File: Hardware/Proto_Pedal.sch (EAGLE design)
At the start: 124 parts, among them J1 POWER_JACKSMD_FIXED, Q1 2.5A/30V, SW1 SWITCH-3PDT

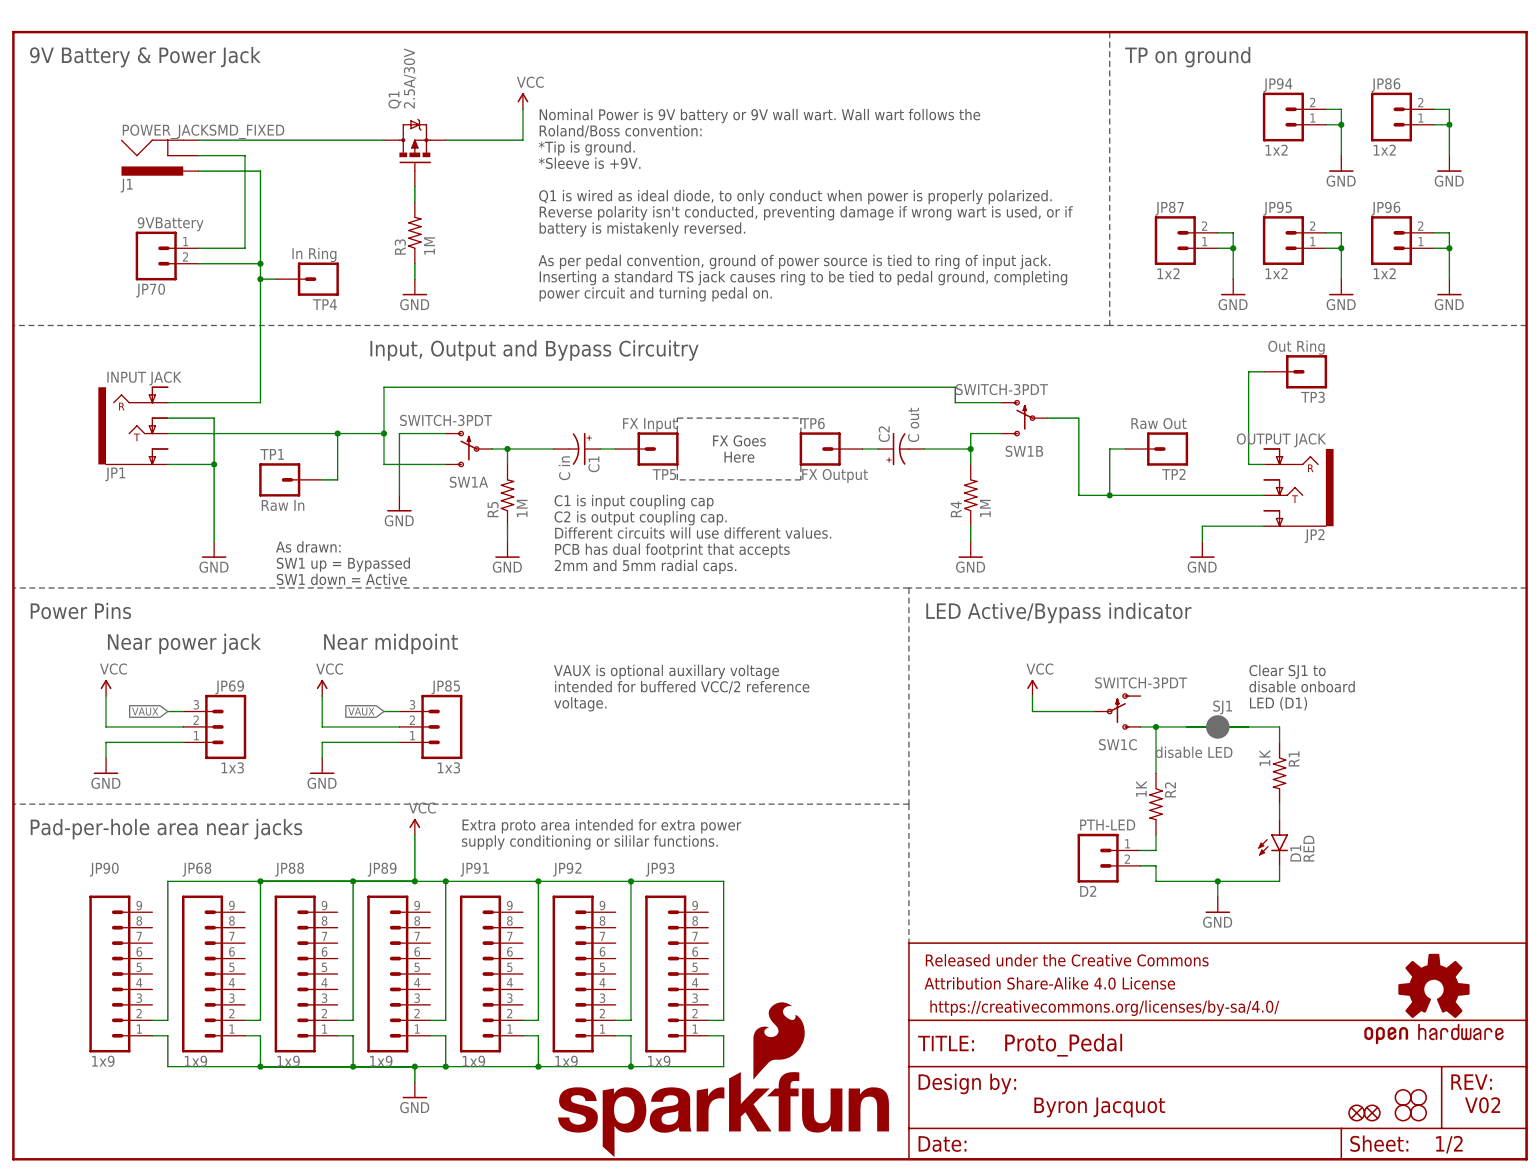
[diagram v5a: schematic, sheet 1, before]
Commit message: Updates after group review.
PTH power connector.
PTH LED bias resistor.
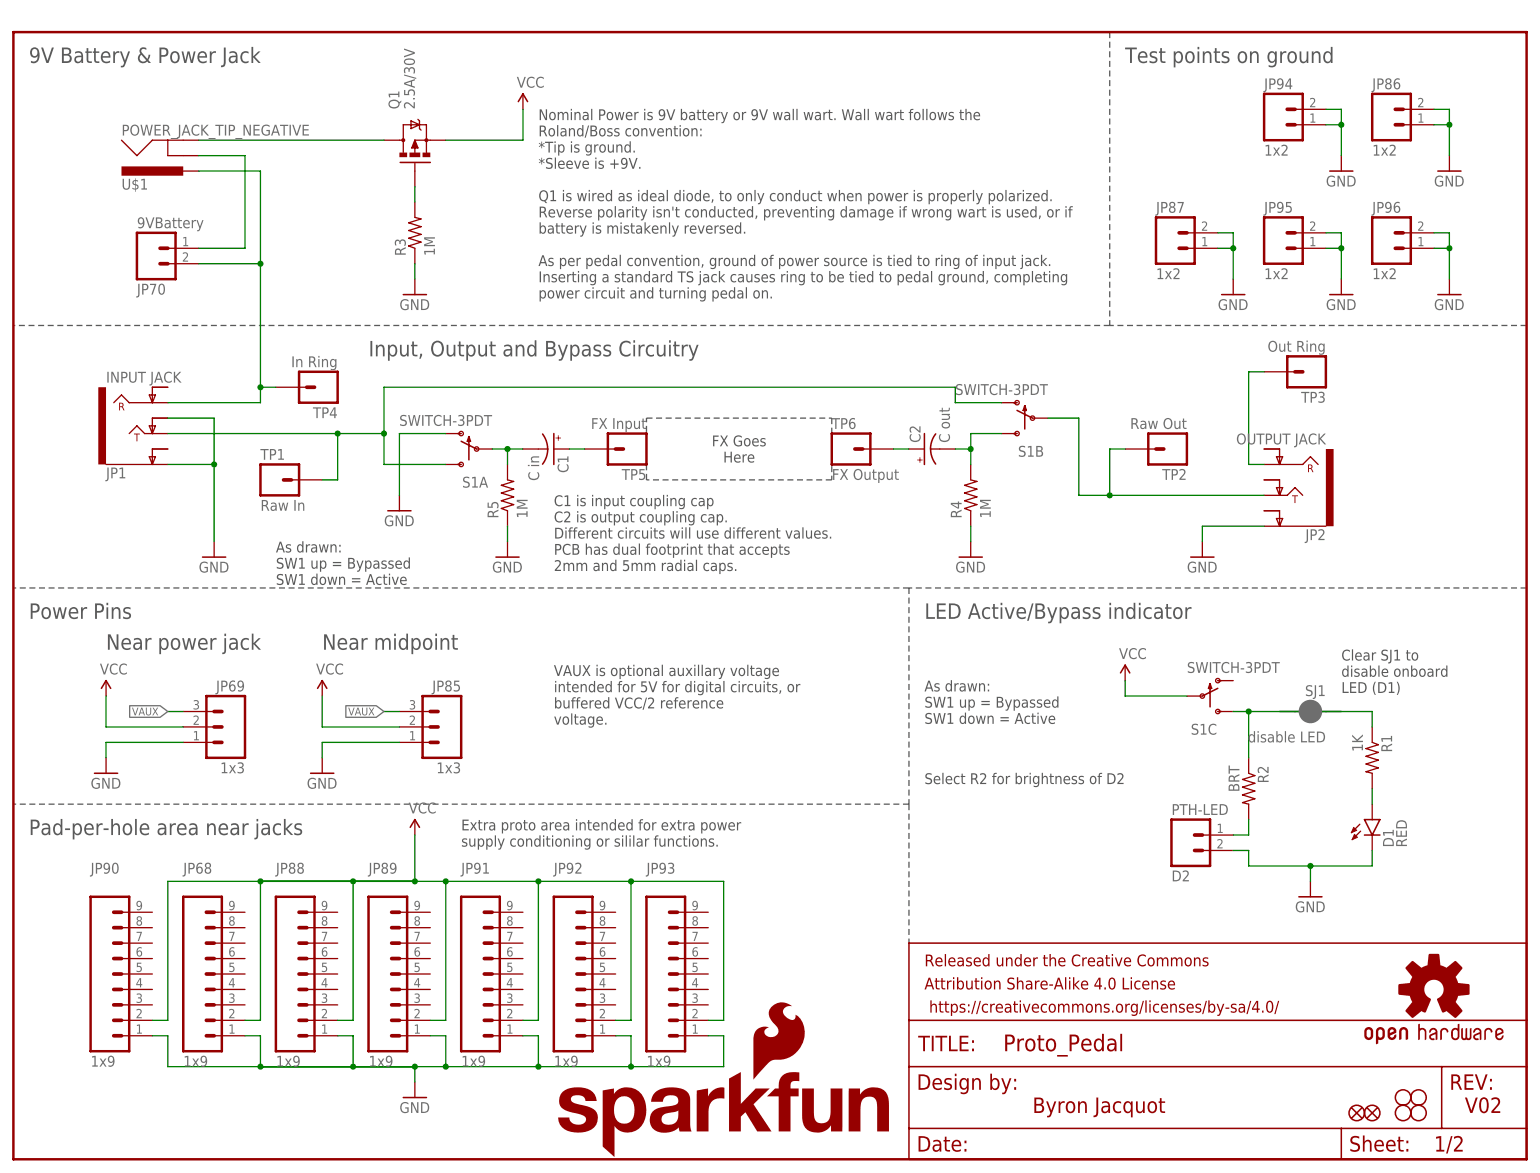
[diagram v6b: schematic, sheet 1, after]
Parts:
- removed J1: POWER_JACKSMD_FIXED, Testing:POWER_JACKSMD_FIXED
- added U$1: POWER_JACK_TIP_NEGATIVE, Testing:POWER_JACK_TIP_NEGATIVE
- R2: value 1K -> BRT; device SparkFun-Resistors:1KOHM-1/10W-1%(0603) -> SparkFun-Resistors:RESISTORAXIAL-0.3
- renumbered SW1 to S1
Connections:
- net N$45: now also U$1.SLEEVEBREAK; no longer J1.GNDBREAK
- net N$55: now also U$1.TIP; no longer J1.PWR
- net VBATT: now also U$1.SLEEVE; no longer J1.GND
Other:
- note added: "Select R2 for brightness of D2"
- note added: "Test points on ground"
- note added: "VAUX is optional auxillary voltage intended for 5V for digital circuits, or buffered VCC/2 reference voltage."
- note removed: "TP on ground"
- note removed: "VAUX is optional auxillary voltage intended for buffered VCC/2 reference voltage."
- moved on the sheet: C1, C2, D1, D2, R1, R2, SJ1, TP4, TP5, TP6

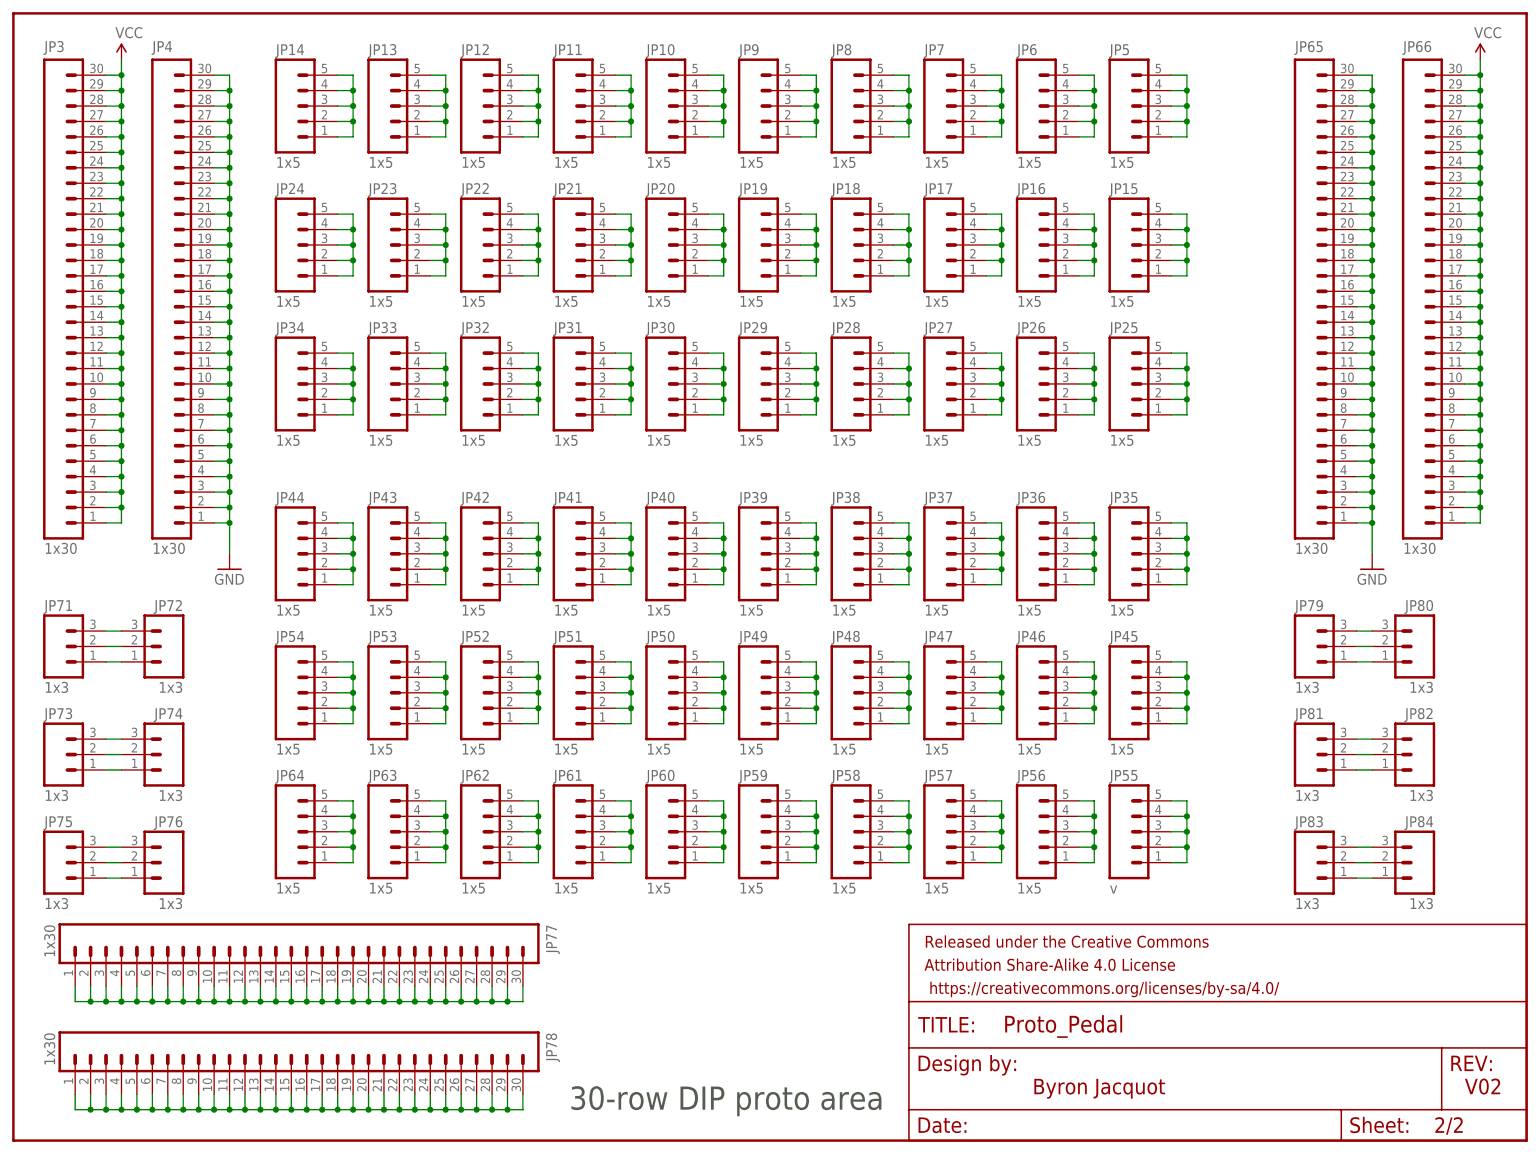
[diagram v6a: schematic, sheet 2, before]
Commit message: Relaxed design to use standard DRU
Fixed funny pour shapes
Relocated a couple traces
Renumbered parts
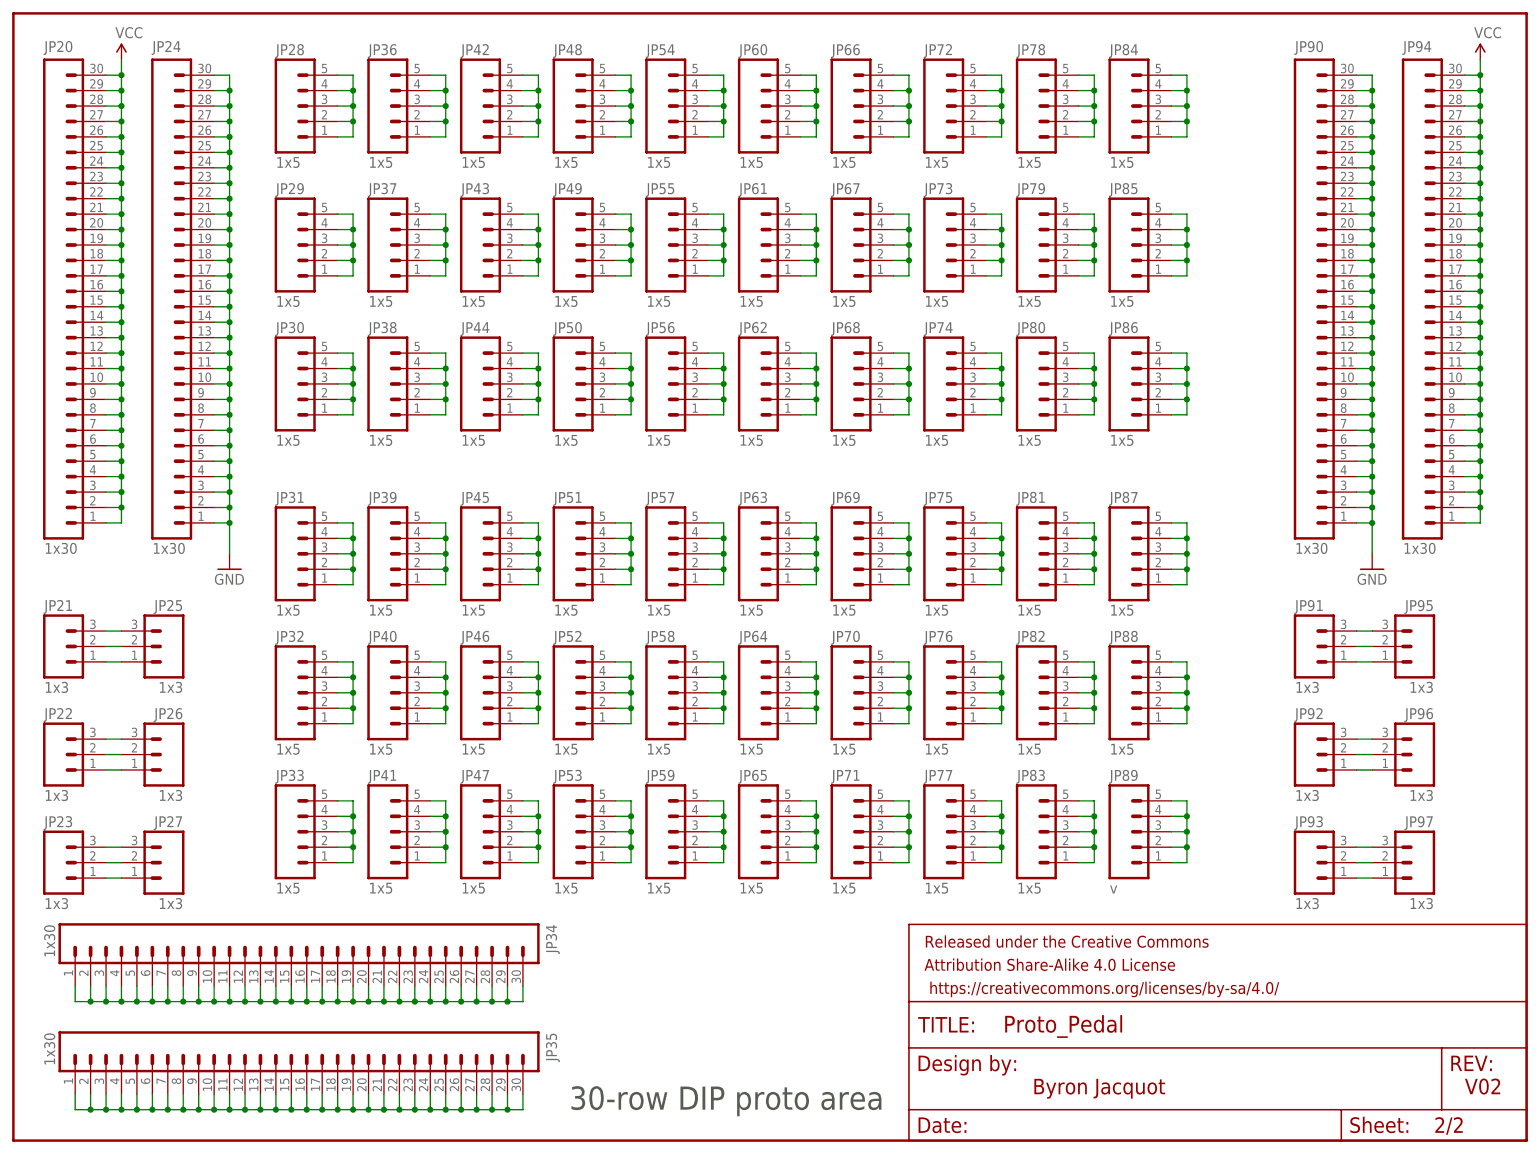
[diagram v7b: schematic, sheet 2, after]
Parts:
- removed D2: PTH-LED, SparkFun-Connectors:M02PTH3
- removed U$1: POWER_JACK_TIP_NEGATIVE, Testing:POWER_JACK_TIP_NEGATIVE
- added JP67: 1x5, SparkFun-Connectors:M05NO_SILK
- added JP97: 1x3, SparkFun-Connectors:M031X03_NO_SILK
- JP1: value INPUT JACK -> 1x9; device SparkFun-Connectors:AUDIO-JACK4-.25-HORIZ-TRS -> SparkFun-Connectors:M09NO_SILK
- JP10, JP11, JP12, JP5, JP7, JP8: value 1x5 -> 1x9; device SparkFun-Connectors:M05NO_SILK -> SparkFun-Connectors:M09NO_SILK
- JP13, JP15, JP16, JP18, JP19: value 1x5 -> 1x2; device SparkFun-Connectors:M05NO_SILK -> SparkFun-Connectors:M021X02_NO_SILK
- JP14: value 1x5 -> PTH-LED; device SparkFun-Connectors:M05NO_SILK -> SparkFun-Connectors:M02PTH3
- JP17: value 1x5 -> OUTPUT JACK; device SparkFun-Connectors:M05NO_SILK -> SparkFun-Connectors:AUDIO-JACK4-.25-HORIZ-TRS
- JP2: value OUTPUT JACK -> INPUT JACK
- JP20, JP24, JP34, JP35: value 1x5 -> 1x30; device SparkFun-Connectors:M05NO_SILK -> SparkFun-Connectors:M30NO_SILK
- JP21, JP22, JP23, JP25, JP26, JP27, JP6, JP9: value 1x5 -> 1x3; device SparkFun-Connectors:M05NO_SILK -> SparkFun-Connectors:M031X03_NO_SILK
- JP3: value 1x30 -> 9VBattery; device SparkFun-Connectors:M30NO_SILK -> SparkFun-Connectors:M02PTH3
- JP4: value 1x30 -> POWER_JACK_TIP_NEGATIVE; device SparkFun-Connectors:M30NO_SILK -> Testing:POWER_JACK_TIP_NEGATIVE
- JP55: value v -> 1x5
- JP65, JP66, JP77, JP78: value 1x30 -> 1x5; device SparkFun-Connectors:M30NO_SILK -> SparkFun-Connectors:M05NO_SILK
- JP68, JP88: value 1x9 -> 1x5; device SparkFun-Connectors:M09NO_SILK -> SparkFun-Connectors:M05NO_SILK
- JP69, JP71, JP72, JP73, JP74, JP75, JP76, JP79, JP80, JP81, JP82, JP83, JP84, JP85: value 1x3 -> 1x5; device SparkFun-Connectors:M031X03_NO_SILK -> SparkFun-Connectors:M05NO_SILK
- JP70: value 9VBattery -> 1x5; device SparkFun-Connectors:M02PTH3 -> SparkFun-Connectors:M05NO_SILK
- JP86, JP87: value 1x2 -> 1x5; device SparkFun-Connectors:M021X02_NO_SILK -> SparkFun-Connectors:M05NO_SILK
- JP89: value 1x9 -> v; device SparkFun-Connectors:M09NO_SILK -> SparkFun-Connectors:M05NO_SILK
- JP90: value 1x9 -> 1x30; device SparkFun-Connectors:M09NO_SILK -> SparkFun-Connectors:M30NO_SILK
- JP91, JP92, JP93: value 1x9 -> 1x3; device SparkFun-Connectors:M09NO_SILK -> SparkFun-Connectors:M031X03_NO_SILK
- JP94: value 1x2 -> 1x30; device SparkFun-Connectors:M021X02_NO_SILK -> SparkFun-Connectors:M30NO_SILK
- JP95, JP96: value 1x2 -> 1x3; device SparkFun-Connectors:M021X02_NO_SILK -> SparkFun-Connectors:M031X03_NO_SILK
- R1: value 1K -> 1M; device SparkFun-Resistors:1KOHM-1/10W-1%(0603) -> SparkFun-Resistors:1MOHM-1/10W-1%(0603)
- R2: value BRT -> 1M; device SparkFun-Resistors:RESISTORAXIAL-0.3 -> SparkFun-Resistors:1MOHM-1/10W-1%(0603)
- R4: value 1M -> BRT; device SparkFun-Resistors:1MOHM-1/10W-1%(0603) -> SparkFun-Resistors:RESISTORAXIAL-0.3
- R5: value 1M -> 1K; device SparkFun-Resistors:1MOHM-1/10W-1%(0603) -> SparkFun-Resistors:1KOHM-1/10W-1%(0603)
- renumbered LOGO3 to LOGO2
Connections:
- removed net N$10 (its old number): JP9.1, JP9.2, JP9.3, JP9.4, JP9.5
- removed net N$11 (its old number): JP11.1, JP11.2, JP11.3, JP11.4, JP11.5
- removed net N$12 (its old number): JP12.1, JP12.2, JP12.3, JP12.4, JP12.5
- removed net N$13 (its old number): JP13.1, JP13.2, JP13.3, JP13.4, JP13.5
- removed net N$14 (its old number): JP14.1, JP14.2, JP14.3, JP14.4, JP14.5
- removed net N$19 (its old number): JP19.1, JP19.2, JP19.3, JP19.4, JP19.5
- removed net N$20 (its old number): JP20.1, JP20.2, JP20.3, JP20.4, JP20.5
- removed net N$21 (its old number): JP21.1, JP21.2, JP21.3, JP21.4, JP21.5
- removed net N$22 (its old number): JP22.1, JP22.2, JP22.3, JP22.4, JP22.5
- removed net N$23 (its old number): JP23.1, JP23.2, JP23.3, JP23.4, JP23.5
- removed net N$24 (its old number): JP24.1, JP24.2, JP24.3, JP24.4, JP24.5
- removed net N$34 (its old number): JP34.1, JP34.2, JP34.3, JP34.4, JP34.5
- removed net N$5 (its old number): JP10.1, JP10.2, JP10.3, JP10.4, JP10.5
- new net N$15: JP89.1, JP89.2, JP89.3, JP89.4, JP89.5
- new net N$28: JP68.1, JP68.2, JP68.3, JP68.4, JP68.5
- new net N$36: JP81.1, JP81.2, JP81.3, JP81.4, JP81.5
- new net N$37: JP75.1, JP75.2, JP75.3, JP75.4, JP75.5
- new net N$38: JP69.1, JP69.2, JP69.3, JP69.4, JP69.5
- new net N$46: JP82.1, JP82.2, JP82.3, JP82.4, JP82.5
- new net N$47: JP76.1, JP76.2, JP76.3, JP76.4, JP76.5
- new net N$48: JP70.1, JP70.2, JP70.3, JP70.4, JP70.5
- new net N$56: JP83.1, JP83.2, JP83.3, JP83.4, JP83.5
- new net N$57: JP77.1, JP77.2, JP77.3, JP77.4, JP77.5
- new net N$58: JP71.1, JP71.2, JP71.3, JP71.4, JP71.5
- new net N$59: JP65.1, JP65.2, JP65.3, JP65.4, JP65.5
- new net N$6: JP88.1, JP88.2, JP88.3, JP88.4, JP88.5
- net FX_IN: now also R2.2; no longer R5.2
- net FX_OUT: now also R3.2; no longer R4.2
- net GND: now also JP1.1, JP10.1, JP11.1, JP12.1, JP13.1, JP13.2, JP14.2, JP15.1, JP15.2, JP16.1, JP16.2, JP17.EARTH, JP18.1, JP18.2, JP19.1, JP19.2, JP2.TIP-NORM, JP24.1, JP24.10, JP24.11, JP24.12, JP24.13, JP24.14, JP24.15, JP24.16, JP24.17, JP24.18, JP24.19, JP24.2, JP24.20, JP24.21, JP24.22, JP24.23, JP24.24, JP24.25, JP24.26, JP24.27, JP24.28, JP24.29, JP24.3, JP24.30, JP24.4, JP24.5, JP24.6, JP24.7, JP24.8, JP24.9, JP5.1, JP6.1, JP7.1, JP8.1, JP9.1, JP90.10, JP90.11, JP90.12, JP90.13, JP90.14, JP90.15, JP90.16, JP90.17, JP90.18, JP90.19, JP90.2, JP90.20, JP90.21, JP90.22, JP90.23, JP90.24, JP90.25, JP90.26, JP90.27, JP90.28, JP90.29, JP90.3, JP90.30, JP90.4, JP90.5, JP90.6, JP90.7, JP90.8, JP90.9, R1.1, R2.1; no longer D2.2, JP1.EARTH, JP1.TIP-NORM, JP4.1, JP4.10, JP4.11, JP4.12, JP4.13, JP4.14, JP4.15, JP4.16, JP4.17, JP4.18, JP4.19, JP4.2, JP4.20, JP4.21, JP4.22, JP4.23, JP4.24, JP4.25, JP4.26, JP4.27, JP4.28, JP4.29, JP4.3, JP4.30, JP4.4, JP4.5, JP4.6, JP4.7, JP4.8, JP4.9, JP65.1, JP65.10, JP65.11, JP65.12, JP65.13, JP65.14, JP65.15, JP65.16, JP65.17, JP65.18, JP65.19, JP65.2, JP65.20, JP65.21, JP65.22, JP65.23, JP65.24, JP65.25, JP65.26, JP65.27, JP65.28, JP65.29, JP65.3, JP65.30, JP65.4, JP65.5, JP65.6, JP65.7, JP65.8, JP65.9, JP68.1, JP69.1, JP85.1, JP86.1, JP86.2, JP87.1, JP87.2, JP88.1, JP89.1, JP91.1, JP92.1, JP93.1, JP94.1, JP94.2, JP95.1, JP95.2, JP96.1, JP96.2, R4.1, R5.1
- net LEDA: now also JP14.1, R4.2; no longer D2.1, R2.2
- net N$1: now also JP84.1, JP84.2, JP84.3, JP84.4, JP84.5; no longer JP5.1, JP5.2, JP5.3, JP5.4, JP5.5
- net N$100: now also JP92.3, JP96.3; no longer JP81.3, JP82.3
- net N$101: now also JP93.1, JP97.1; no longer JP83.1, JP84.1
- net N$102: now also JP93.2, JP97.2; no longer JP83.2, JP84.2
- net N$103: now also JP93.3, JP97.3; no longer JP83.3, JP84.3
- net N$16: now also JP79.1, JP79.2, JP79.3, JP79.4, JP79.5; no longer JP16.1, JP16.2, JP16.3, JP16.4, JP16.5
- net N$17: now also JP73.1, JP73.2, JP73.3, JP73.4, JP73.5; no longer JP17.1, JP17.2, JP17.3, JP17.4, JP17.5
- net N$18: now also JP67.1, JP67.2, JP67.3, JP67.4, JP67.5; no longer JP18.1, JP18.2, JP18.3, JP18.4, JP18.5
- net N$2: now also JP85.1, JP85.2, JP85.3, JP85.4, JP85.5; no longer JP15.1, JP15.2, JP15.3, JP15.4, JP15.5
- net N$25: now also R5.2; no longer R1.2
- net N$26: now also JP80.1, JP80.2, JP80.3, JP80.4, JP80.5; no longer JP26.1, JP26.2, JP26.3, JP26.4, JP26.5
- net N$27: now also JP74.1, JP74.2, JP74.3, JP74.4, JP74.5; no longer JP27.1, JP27.2, JP27.3, JP27.4, JP27.5
- net N$3: now also JP86.1, JP86.2, JP86.3, JP86.4, JP86.5; no longer JP25.1, JP25.2, JP25.3, JP25.4, JP25.5
- net N$35: now also R4.1; no longer R2.1
- net N$4: now also JP87.1, JP87.2, JP87.3, JP87.4, JP87.5; no longer JP35.1, JP35.2, JP35.3, JP35.4, JP35.5
- net N$45: now also JP3.1, JP4.SLEEVEBREAK; no longer JP70.1, U$1.SLEEVEBREAK
- net N$55: now also JP2.RING, JP3.2, JP4.TIP; no longer JP1.RING, JP70.2, U$1.TIP
- net N$65: now also R5.1; no longer R1.1
- net N$66: now also JP17.RING; no longer JP2.RING
- net N$7: now also JP78.1, JP78.2, JP78.3, JP78.4, JP78.5; no longer JP6.1, JP6.2, JP6.3, JP6.4, JP6.5
- net N$70: now also JP2.TIP; no longer JP1.TIP
- net N$71: now also JP17.TIP; no longer JP2.TIP
- net N$75: now also R1.2; no longer R3.2
- net N$77: now also JP21.1, JP25.1; no longer JP71.1, JP72.1
- net N$79: now also JP21.2, JP25.2; no longer JP71.2, JP72.2
- net N$8: now also JP72.1, JP72.2, JP72.3, JP72.4, JP72.5; no longer JP7.1, JP7.2, JP7.3, JP7.4, JP7.5
- net N$81: now also JP21.3, JP25.3; no longer JP71.3, JP72.3
- net N$83: now also JP22.1, JP26.1; no longer JP73.1, JP74.1
- net N$85: now also JP22.2, JP26.2; no longer JP73.2, JP74.2
- net N$87: now also JP22.3, JP26.3; no longer JP73.3, JP74.3
- net N$89: now also JP34.1, JP34.10, JP34.11, JP34.12, JP34.13, JP34.14, JP34.15, JP34.16, JP34.17, JP34.18, JP34.19, JP34.2, JP34.20, JP34.21, JP34.22, JP34.23, JP34.24, JP34.25, JP34.26, JP34.27, JP34.28, JP34.29, JP34.3, JP34.30, JP34.4, JP34.5, JP34.6, JP34.7, JP34.8, JP34.9; no longer JP77.1, JP77.10, JP77.11, JP77.12, JP77.13, JP77.14, JP77.15, JP77.16, JP77.17, JP77.18, JP77.19, JP77.2, JP77.20, JP77.21, JP77.22, JP77.23, JP77.24, JP77.25, JP77.26, JP77.27, JP77.28, JP77.29, JP77.3, JP77.30, JP77.4, JP77.5, JP77.6, JP77.7, JP77.8, JP77.9
- net N$9: now also JP66.1, JP66.2, JP66.3, JP66.4, JP66.5; no longer JP8.1, JP8.2, JP8.3, JP8.4, JP8.5
- net N$90: now also JP35.1, JP35.10, JP35.11, JP35.12, JP35.13, JP35.14, JP35.15, JP35.16, JP35.17, JP35.18, JP35.19, JP35.2, JP35.20, JP35.21, JP35.22, JP35.23, JP35.24, JP35.25, JP35.26, JP35.27, JP35.28, JP35.29, JP35.3, JP35.30, JP35.4, JP35.5, JP35.6, JP35.7, JP35.8, JP35.9; no longer JP78.1, JP78.10, JP78.11, JP78.12, JP78.13, JP78.14, JP78.15, JP78.16, JP78.17, JP78.18, JP78.19, JP78.2, JP78.20, JP78.21, JP78.22, JP78.23, JP78.24, JP78.25, JP78.26, JP78.27, JP78.28, JP78.29, JP78.3, JP78.30, JP78.4, JP78.5, JP78.6, JP78.7, JP78.8, JP78.9
- net N$91: now also JP23.1, JP27.1; no longer JP75.1, JP76.1
- net N$93: now also JP23.2, JP27.2; no longer JP75.2, JP76.2
- net N$94: now also JP23.3, JP27.3; no longer JP75.3, JP76.3
- net N$95: now also JP91.1, JP95.1; no longer JP79.1, JP80.1
- net N$96: now also JP91.2, JP95.2; no longer JP79.2, JP80.2
- net N$97: now also JP91.3, JP95.3; no longer JP79.3, JP80.3
- net N$98: now also JP92.1, JP96.1; no longer JP81.1, JP82.1
- net N$99: now also JP92.2, JP96.2; no longer JP81.2, JP82.2
- net VAUX: now also JP6.3, JP9.3; no longer JP69.3, JP85.3
- net VBATT: now also JP4.SLEEVE; no longer U$1.SLEEVE
- net VCC: now also JP1.2, JP10.2, JP11.2, JP12.2, JP20.1, JP20.10, JP20.11, JP20.12, JP20.13, JP20.14, JP20.15, JP20.16, JP20.17, JP20.18, JP20.19, JP20.2, JP20.20, JP20.21, JP20.22, JP20.23, JP20.24, JP20.25, JP20.26, JP20.27, JP20.28, JP20.29, JP20.3, JP20.30, JP20.4, JP20.5, JP20.6, JP20.7, JP20.8, JP20.9, JP5.2, JP6.2, JP7.2, JP8.2, JP9.2, JP94.1, JP94.10, JP94.11, JP94.12, JP94.13, JP94.14, JP94.15, JP94.16, JP94.17, JP94.18, JP94.19, JP94.2, JP94.20, JP94.21, JP94.22, JP94.23, JP94.24, JP94.25, JP94.26, JP94.27, JP94.28, JP94.29, JP94.3, JP94.30, JP94.4, JP94.5, JP94.6, JP94.7, JP94.8, JP94.9; no longer JP3.1, JP3.10, JP3.11, JP3.12, JP3.13, JP3.14, JP3.15, JP3.16, JP3.17, JP3.18, JP3.19, JP3.2, JP3.20, JP3.21, JP3.22, JP3.23, JP3.24, JP3.25, JP3.26, JP3.27, JP3.28, JP3.29, JP3.3, JP3.30, JP3.4, JP3.5, JP3.6, JP3.7, JP3.8, JP3.9, JP66.1, JP66.10, JP66.11, JP66.12, JP66.13, JP66.14, JP66.15, JP66.16, JP66.17, JP66.18, JP66.19, JP66.2, JP66.20, JP66.21, JP66.22, JP66.23, JP66.24, JP66.25, JP66.26, JP66.27, JP66.28, JP66.29, JP66.3, JP66.30, JP66.4, JP66.5, JP66.6, JP66.7, JP66.8, JP66.9, JP68.2, JP69.2, JP85.2, JP88.2, JP89.2, JP90.2, JP91.2, JP92.2, JP93.2
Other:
- note added: "Nominal Power is 9V battery or 9V wall wart. Wall wart follows the Roland/Boss convention: *Tip is ground. *Sleeve is +9V. Plugging in to the barrel jack takes the battery out of circuit by lifting the sleeve normal. Q1 is wired as ideal diode, to only conduct when power is properly polarized. Reverse polarity isn't conducted, preventing damage if wrong wart is used, or if battery is mistakenly r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"
- note added: "VAUX is optional auxillary voltage intended for 3.3V or 5V for digital circuits, or buffered VCC/2 reference voltage."
- note removed: "Nominal Power is 9V battery or 9V wall wart. Wall wart follows the Roland/Boss convention: *Tip is ground. *Sleeve is +9V. Q1 is wired as ideal diode, to only conduct when power is properly polarized. Reverse polarity isn't conducted, preventing damage if wrong wart is used, or if battery is mistakenly reversed. As per pedal convention, ground of power source is tied to ring of input jack. Insert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"
- note removed: "VAUX is optional auxillary voltage intended for 5V for digital circuits, or buffered VCC/2 reference voltage."
- moved on the sheet: JP1, JP2, JP28, JP29, JP30, JP31, JP32, JP33, JP36, JP37, JP38, JP39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
